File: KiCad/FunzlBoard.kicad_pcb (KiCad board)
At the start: 2 copper layers, 10 parts

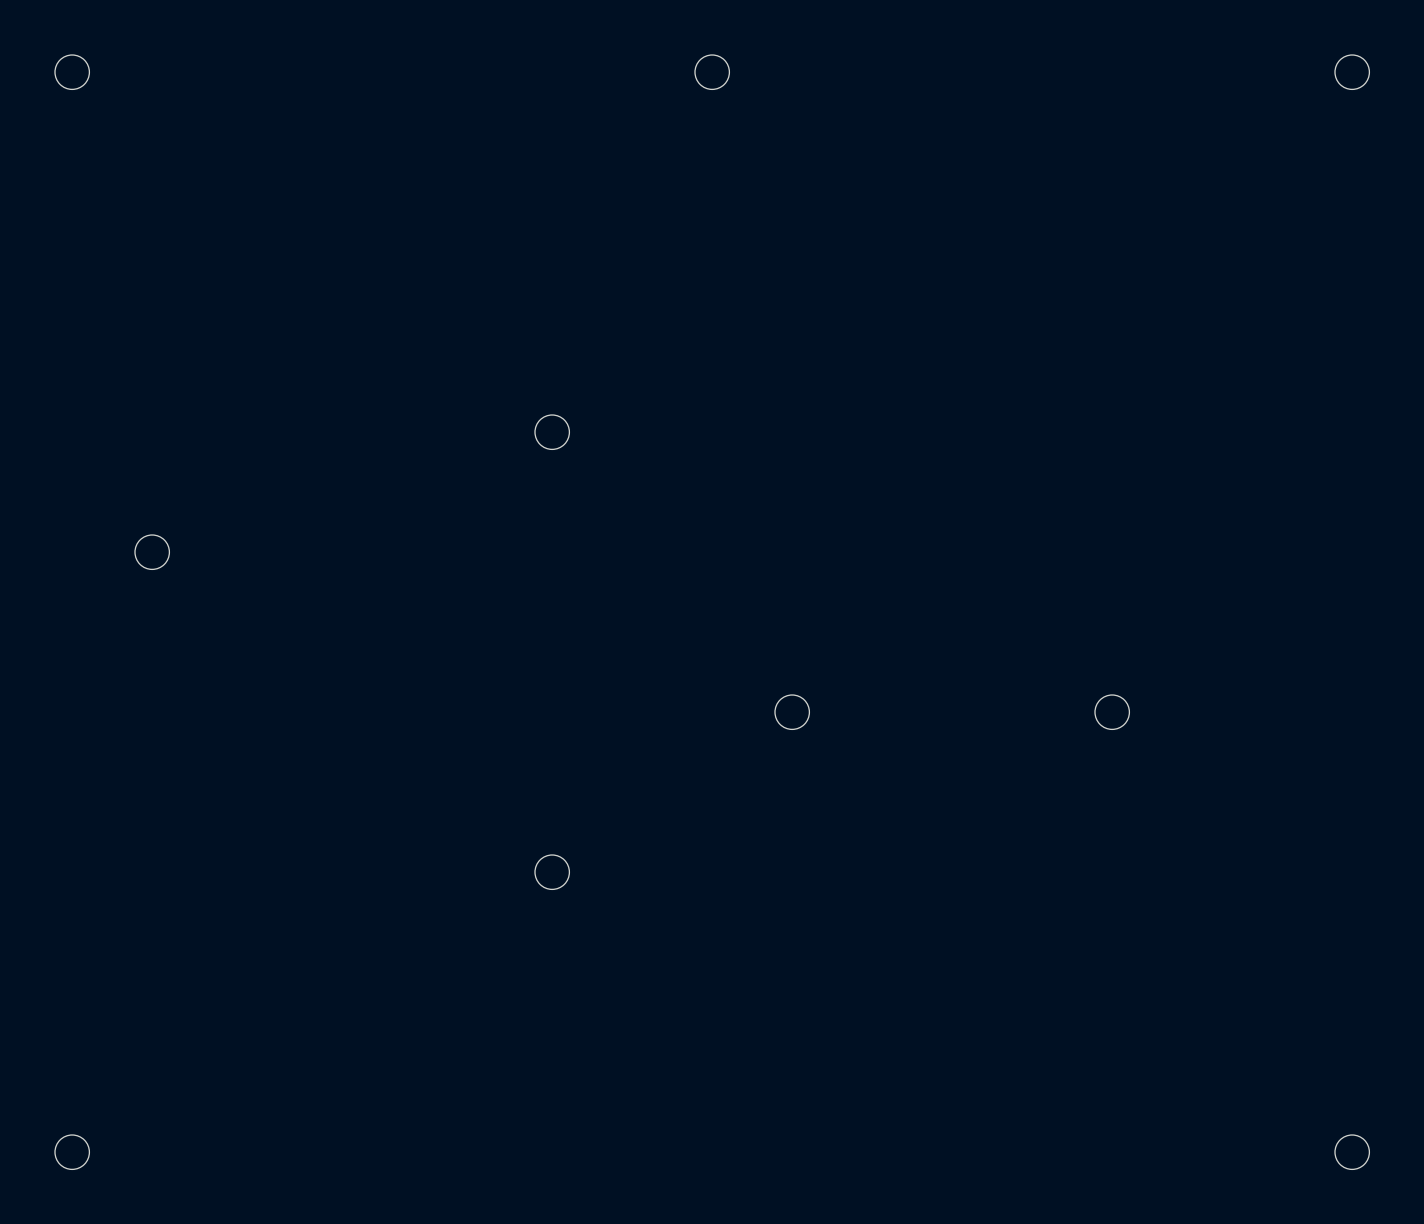
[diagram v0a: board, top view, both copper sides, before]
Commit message: Show mainboard in OpenSCAD
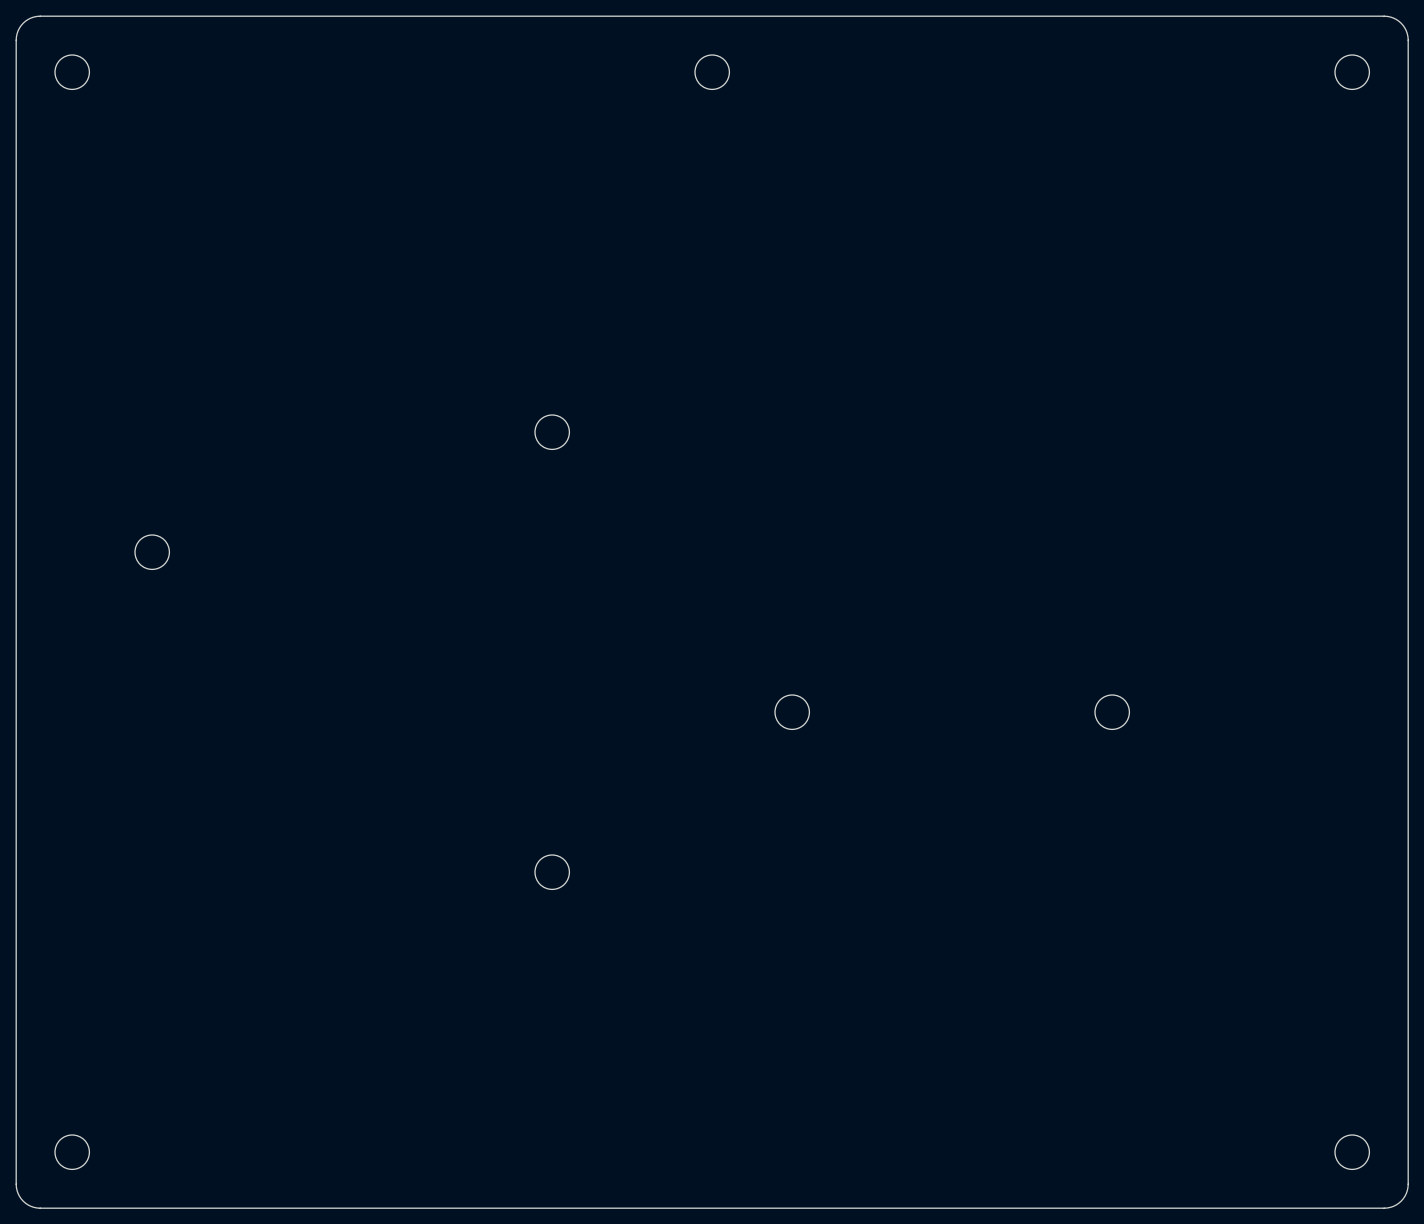
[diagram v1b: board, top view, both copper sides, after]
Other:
- board outline added: 174 x 149 mm
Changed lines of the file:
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@@
 		(embedded_fonts no)
+	)
+	(gr_line
+		(start 177 6)
+		(end 177 149)
+		(stroke
+			(width 0.05)
+			(type default)
+		)
+		(layer "Edge.Cuts")
+	)
+	(gr_arc
+		(start 174 3)
+		(mid 176.12132 3.87868)
+		(end 177 6)
+		(stroke
+			(width 0.05)
+			(type default)
+		)
+		(layer "Edge.Cuts")
+	)
+	(gr_arc
+		(start 6 152)
+		(mid 3.87868 151.12132)
+		(end 3 149)
+		(stroke
+			(width 0.05)
+			(type default)
+		)
+		(layer "Edge.Cuts")
+	)
+	(gr_line
+		(start 6 3)
+		(end 174 3)
+		(stroke
+			(width 0.05)
+			(type default)
+		)
+		(layer "Edge.Cuts")
+	)
+	(gr_arc
+		(start 3 6)
+		(mid 3.87868 3.87868)
+		(end 6 3)
+		(stroke
+			(width 0.05)
+			(type default)
+		)
+		(layer "Edge.Cuts")
+	)
+	(gr_line
+		(start 174 152)
+		(end 6 152)
+		(stroke
+			(width 0.05)
+			(type default)
+		)
+		(layer "Edge.Cuts")
+	)
+	(gr_arc
+		(start 177 149)
+		(mid 176.12132 151.12132)
+		(end 174 152)
+		(stroke
+			(width 0.05)
+			(type default)
+		)
+		(layer "Edge.Cuts")
+	)
+	(gr_line
+		(start 3 149)
+		(end 3 6)
+		(stroke
+			(width 0.05)
+			(type default)
+		)
+		(layer "Edge.Cuts")
+	)
+	(gr_rect
+		(start 0 0)
+		(end 180 155)
+		(stroke
+			(width 0.1)
+			(type default)
+		)
+		(fill no)
+		(layer "User.2")
 	)
 	(embedded_fonts no)

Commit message: Cut out for battery
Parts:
- added D1: WS2812B, LED_SMD:LED_WS2812B_PLCC4_5.0x5.0mm_P3.2mm, F.Cu at (160.0, 68.0)
- added D10: WS2812B, LED_SMD:LED_WS2812B_PLCC4_5.0x5.0mm_P3.2mm, F.Cu at (246.4, 100.1)
- added D11: WS2812B, LED_SMD:LED_WS2812B_PLCC4_5.0x5.0mm_P3.2mm, F.Cu at (254.6, 47.2)
- added D12: WS2812B, LED_SMD:LED_WS2812B_PLCC4_5.0x5.0mm_P3.2mm, F.Cu at (254.6, 53.8)
- added D13: WS2812B, LED_SMD:LED_WS2812B_PLCC4_5.0x5.0mm_P3.2mm, F.Cu at (254.6, 60.4)
- added D14: WS2812B, LED_SMD:LED_WS2812B_PLCC4_5.0x5.0mm_P3.2mm, F.Cu at (254.6, 67.0)
- added D15: WS2812B, LED_SMD:LED_WS2812B_PLCC4_5.0x5.0mm_P3.2mm, F.Cu at (254.6, 73.7)
- added D16: WS2812B, LED_SMD:LED_WS2812B_PLCC4_5.0x5.0mm_P3.2mm, F.Cu at (254.6, 80.3)
- added D17: WS2812B, LED_SMD:LED_WS2812B_PLCC4_5.0x5.0mm_P3.2mm, F.Cu at (254.6, 86.9)
- added D18: WS2812B, LED_SMD:LED_WS2812B_PLCC4_5.0x5.0mm_P3.2mm, F.Cu at (254.6, 93.5)
- added D19: WS2812B, LED_SMD:LED_WS2812B_PLCC4_5.0x5.0mm_P3.2mm, F.Cu at (254.6, 100.1)
- added D2: WS2812B, LED_SMD:LED_WS2812B_PLCC4_5.0x5.0mm_P3.2mm, B.Cu at (20.0, 86.0)
- added D20: WS2812B, LED_SMD:LED_WS2812B_PLCC4_5.0x5.0mm_P3.2mm, F.Cu at (262.7, 47.2)
- added D21: WS2812B, LED_SMD:LED_WS2812B_PLCC4_5.0x5.0mm_P3.2mm, F.Cu at (262.7, 53.8)
- added D22: WS2812B, LED_SMD:LED_WS2812B_PLCC4_5.0x5.0mm_P3.2mm, F.Cu at (262.7, 60.4)
- added D23: WS2812B, LED_SMD:LED_WS2812B_PLCC4_5.0x5.0mm_P3.2mm, F.Cu at (262.7, 67.0)
- added D24: WS2812B, LED_SMD:LED_WS2812B_PLCC4_5.0x5.0mm_P3.2mm, F.Cu at (262.7, 73.7)
- added D25: WS2812B, LED_SMD:LED_WS2812B_PLCC4_5.0x5.0mm_P3.2mm, F.Cu at (262.7, 80.3)
- added D26: WS2812B, LED_SMD:LED_WS2812B_PLCC4_5.0x5.0mm_P3.2mm, F.Cu at (262.7, 86.9)
- added D27: WS2812B, LED_SMD:LED_WS2812B_PLCC4_5.0x5.0mm_P3.2mm, F.Cu at (262.7, 93.5)
- added D28: WS2812B, LED_SMD:LED_WS2812B_PLCC4_5.0x5.0mm_P3.2mm, F.Cu at (262.7, 100.1)
- added D29: WS2812B, LED_SMD:LED_WS2812B_PLCC4_5.0x5.0mm_P3.2mm, F.Cu at (270.8, 47.2)
- added D3: WS2812B, LED_SMD:LED_WS2812B_PLCC4_5.0x5.0mm_P3.2mm, B.Cu at (38.0, 86.0)
- added D30: WS2812B, LED_SMD:LED_WS2812B_PLCC4_5.0x5.0mm_P3.2mm, F.Cu at (270.8, 53.8)
- added D31: WS2812B, LED_SMD:LED_WS2812B_PLCC4_5.0x5.0mm_P3.2mm, F.Cu at (270.8, 60.4)
- added D32: WS2812B, LED_SMD:LED_WS2812B_PLCC4_5.0x5.0mm_P3.2mm, F.Cu at (270.8, 67.0)
- added D33: WS2812B, LED_SMD:LED_WS2812B_PLCC4_5.0x5.0mm_P3.2mm, F.Cu at (270.8, 73.7)
- added D34: WS2812B, LED_SMD:LED_WS2812B_PLCC4_5.0x5.0mm_P3.2mm, F.Cu at (270.8, 80.3)
- added D35: WS2812B, LED_SMD:LED_WS2812B_PLCC4_5.0x5.0mm_P3.2mm, F.Cu at (270.8, 86.9)
- added D36: WS2812B, LED_SMD:LED_WS2812B_PLCC4_5.0x5.0mm_P3.2mm, F.Cu at (270.8, 93.5)
- added D37: WS2812B, LED_SMD:LED_WS2812B_PLCC4_5.0x5.0mm_P3.2mm, F.Cu at (270.8, 100.1)
- added D38: WS2812B, LED_SMD:LED_WS2812B_PLCC4_5.0x5.0mm_P3.2mm, F.Cu at (278.9, 47.2)
- added D39: WS2812B, LED_SMD:LED_WS2812B_PLCC4_5.0x5.0mm_P3.2mm, F.Cu at (278.9, 53.8)
- added D4: WS2812B, LED_SMD:LED_WS2812B_PLCC4_5.0x5.0mm_P3.2mm, B.Cu at (56.0, 86.0)
- added D40: WS2812B, LED_SMD:LED_WS2812B_PLCC4_5.0x5.0mm_P3.2mm, F.Cu at (278.9, 60.4)
- added D41: WS2812B, LED_SMD:LED_WS2812B_PLCC4_5.0x5.0mm_P3.2mm, F.Cu at (278.9, 67.0)
- added D42: WS2812B, LED_SMD:LED_WS2812B_PLCC4_5.0x5.0mm_P3.2mm, F.Cu at (278.9, 73.7)
- added D43: WS2812B, LED_SMD:LED_WS2812B_PLCC4_5.0x5.0mm_P3.2mm, F.Cu at (278.9, 80.3)
- added D44: WS2812B, LED_SMD:LED_WS2812B_PLCC4_5.0x5.0mm_P3.2mm, F.Cu at (278.9, 86.9)
- added D5: WS2812B, LED_SMD:LED_WS2812B_PLCC4_5.0x5.0mm_P3.2mm, F.Cu at (246.4, 67.0)
- added D6: WS2812B, LED_SMD:LED_WS2812B_PLCC4_5.0x5.0mm_P3.2mm, F.Cu at (246.4, 73.7)
- added D7: WS2812B, LED_SMD:LED_WS2812B_PLCC4_5.0x5.0mm_P3.2mm, F.Cu at (246.4, 80.3)
- added D8: WS2812B, LED_SMD:LED_WS2812B_PLCC4_5.0x5.0mm_P3.2mm, F.Cu at (246.4, 86.9)
- added D9: WS2812B, LED_SMD:LED_WS2812B_PLCC4_5.0x5.0mm_P3.2mm, F.Cu at (246.4, 93.5)
- moved H9 135.0 mm to (90.0, 145.0)
- moved H10 65.0 mm to (70.0, 45.0)
- moved H6 45.0 mm to (70.0, 100.0)
- moved H8 25.0 mm to (140.0, 65.0)
- moved H7 15.0 mm to (20.0, 85.0)
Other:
- outline, holes or cut-outs redrawn

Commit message: .
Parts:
- D2, D3, D4: moved to F.Cu
- moved H5 25.0 mm to (100.0, 65.0)
- moved D2 20.0 mm to (20.0, 66.0), turned to 0 degrees
- moved D3 20.0 mm to (38.0, 66.0), turned to 0 degrees
- moved D4 20.0 mm to (56.0, 66.0), turned to 0 degrees

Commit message: Align LEDs on main board
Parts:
- added D45: WS2812B, LED_SMD:LED_WS2812B_PLCC4_5.0x5.0mm_P3.2mm, F.Cu at (279.6, 93.3)
- added U1: ESP32-C3_SUPERMINI_SMD, Lib:MODULE_ESP32-C3_SUPERMINI, B.Cu at (14.9, 25.0)
- moved D9 232.0 mm to (20.0, 144.0)
- moved D8 228.3 mm to (20.0, 116.0)
- moved D7 228.2 mm to (19.3, 102.0)
- moved D11 225.3 mm to (40.0, 116.0)
- moved D12 212.1 mm to (50.0, 110.0)
- moved D10 211.0 mm to (40.0, 144.0)
- moved D14 209.2 mm to (60.0, 144.0)
- moved D6 206.0 mm to (40.7, 84.0)
- moved D13 202.3 mm to (60.0, 116.0)
- moved D37 194.0 mm to (81.5, 57.4)
- moved D38 193.1 mm to (85.9, 50.9)
- moved D36 192.9 mm to (80.0, 65.0)
- moved D5 190.5 mm to (56.6, 83.0)
- moved D35 189.8 mm to (81.5, 72.7)
- moved D39 186.7 mm to (92.3, 46.5)
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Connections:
- D1 pad 4: unconnected-(D1-DIN-Pad4) -> Net-(D1-DIN)
- D44 pad 2: unconnected-(D44-DOUT-Pad2) -> Net-(D44-DOUT)
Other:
- outline, holes or cut-outs redrawn

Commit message: .
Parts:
- removed D44, D45: WS2812B, LED_SMD:LED_WS2812B_PLCC4_5.0x5.0mm_P3.2mm
- D1: moved to B.Cu
- turned D1 to 180 degrees
- turned D29 to -22.5 degrees
- turned D30 to -45 degrees
- turned D31 to -67.5 degrees
- turned D32 to -90 degrees
- turned D33 to -112.5 degrees
- turned D34 to -135 degrees
- turned D35 to -157.5 degrees
- turned D36 to 180 degrees
- turned D37 to 157.5 degrees
- turned D38 to 135 degrees
- turned D39 to 112.5 degrees
- turned D40 to 90 degrees
- turned D41 to 67.5 degrees
- turned D42 to 45 degrees
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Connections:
- D43 pad 2: Net-(D43-DOUT) -> unconnected-(D43-DOUT-Pad2)
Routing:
- net GND: track 0.00 -> 156.4 mm, vias 0 -> 16
- net Net-(D27-DOUT): track 0.00 -> 24.6 mm
- net Net-(D1-DIN): track 0.00 -> 13.6 mm
- net Net-(D29-DOUT): track 0.00 -> 7.08 mm
- net Net-(D37-DOUT): track 0.00 -> 7.07 mm
- net Net-(D41-DOUT): track 0.00 -> 7.07 mm
- net Net-(D33-DOUT): track 0.00 -> 7.07 mm
- net Net-(D35-DOUT): track 0.00 -> 7.07 mm
- net Net-(D31-DOUT): track 0.00 -> 7.07 mm
- net Net-(D39-DOUT): track 0.00 -> 7.07 mm
- net Net-(D34-DOUT): track 0.00 -> 7.01 mm
- net Net-(D38-DOUT): track 0.00 -> 7.01 mm
- net Net-(D42-DOUT): track 0.00 -> 7.01 mm
- net Net-(D40-DOUT): track 0.00 -> 7.00 mm
- net Net-(D32-DOUT): track 0.00 -> 7.00 mm
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- added copper zone on F.Cu, net +5V
- added copper zone on B.Cu, net GND
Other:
- outline, holes or cut-outs redrawn

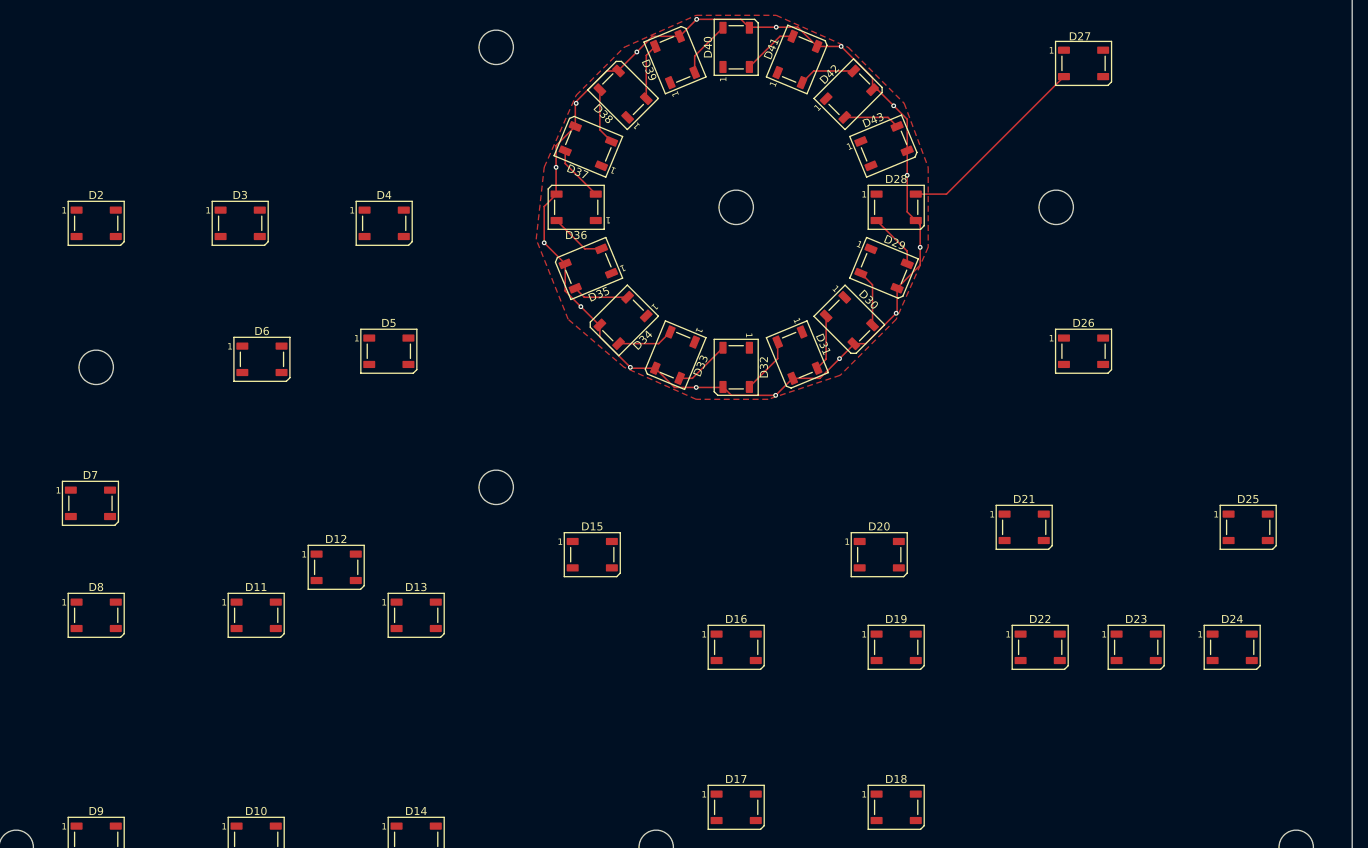
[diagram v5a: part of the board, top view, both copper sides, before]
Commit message: Cut out board for components
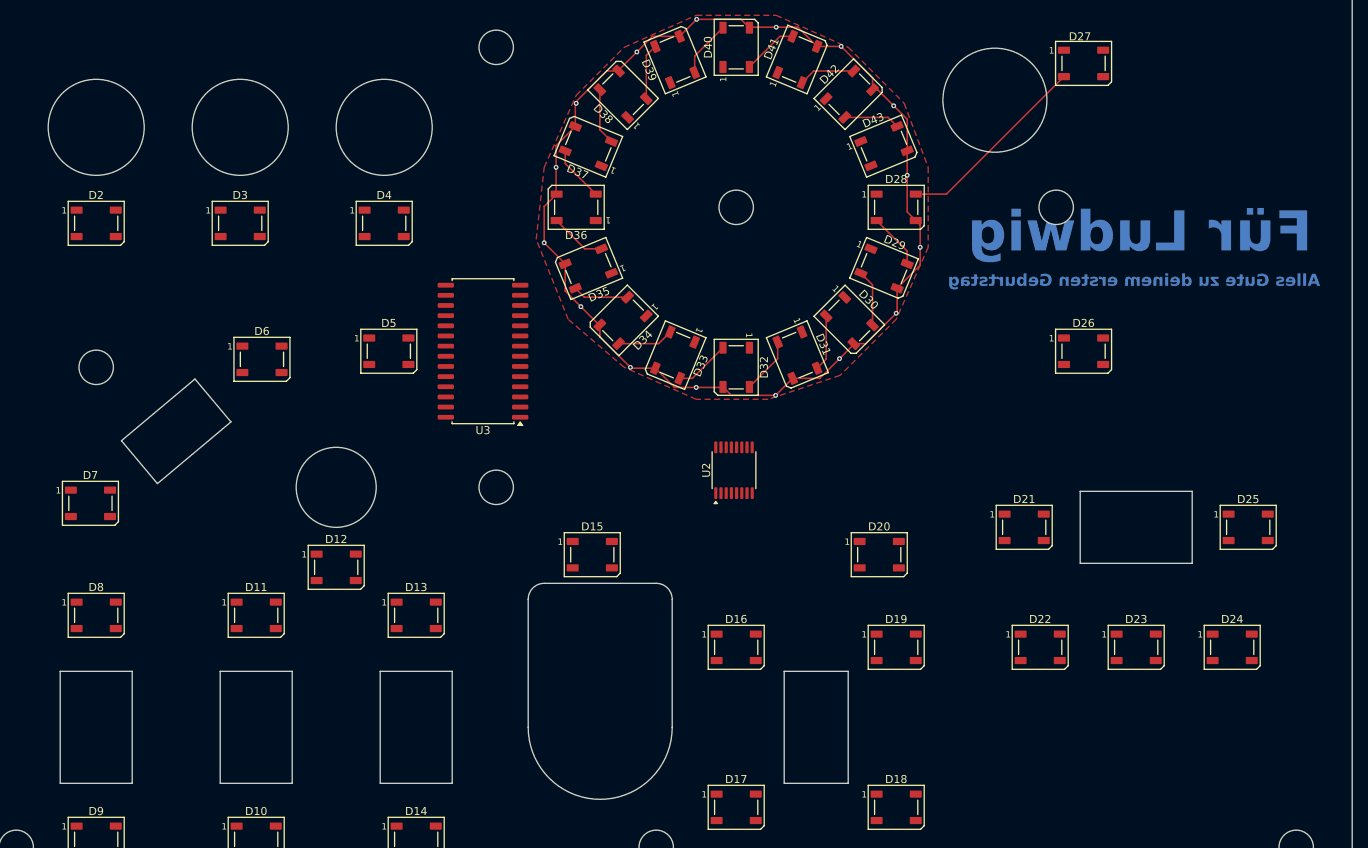
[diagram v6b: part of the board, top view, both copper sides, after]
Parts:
- added U2: ADS7828, Package_SO:TSSOP-16_4.4x5mm_P0.65mm, F.Cu at (99.7, 97.9)
- added U3: MCP23017_SO, Package_SO:SOIC-28W_7.5x17.9mm_P1.27mm, F.Cu at (68.3, 83.0)
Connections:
- U1 pad 8: unconnected-(U1-GPIO8-Pad8) -> SDA
- U1 pad 9: unconnected-(U1-GPIO9-Pad9) -> SCL
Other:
- outline, holes or cut-outs redrawn
- board text added: "Alles Gute zu deinem ersten Geburtstag"
- board text added: "Für Ludwig"
